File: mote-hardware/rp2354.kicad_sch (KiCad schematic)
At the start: 32 parts, among them J4 SM03B-SRSS-TB, J6 Conn_01x03_Pin, SW1 SW_Push, SW2 SW_Push, U1 RP2350_60QFN, U4 RP Radio Module 2, Y1 ABM8-272-T3

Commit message: Finish routing
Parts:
- J4: footprint Connector_JST:JST_SH_SM03B-SRSS-TB_1x03-1MP_P1.00mm_Horizontal -> Connector_JST:JST_SH_BM03B-SRSS-TB_1x03-1MP_P1.00mm_Vertical
- U1: value RP2350_60QFN -> RP2354_60QFN
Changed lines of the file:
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@@
 			)
 		)
-		(property "Value" "RP2350_60QFN"
+		(property "Value" "RP2354_60QFN"
 			(at 131.6833 172.72 0)
 			(effects
@@
 			)
 		)
-		(property "Footprint" "Connector_JST:JST_SH_SM03B-SRSS-TB_1x03-1MP_P1.00mm_Horizontal"
+		(property "Footprint" "Connector_JST:JST_SH_BM03B-SRSS-TB_1x03-1MP_P1.00mm_Vertical"
 			(at 294.64 213.36 0)
 			(effects

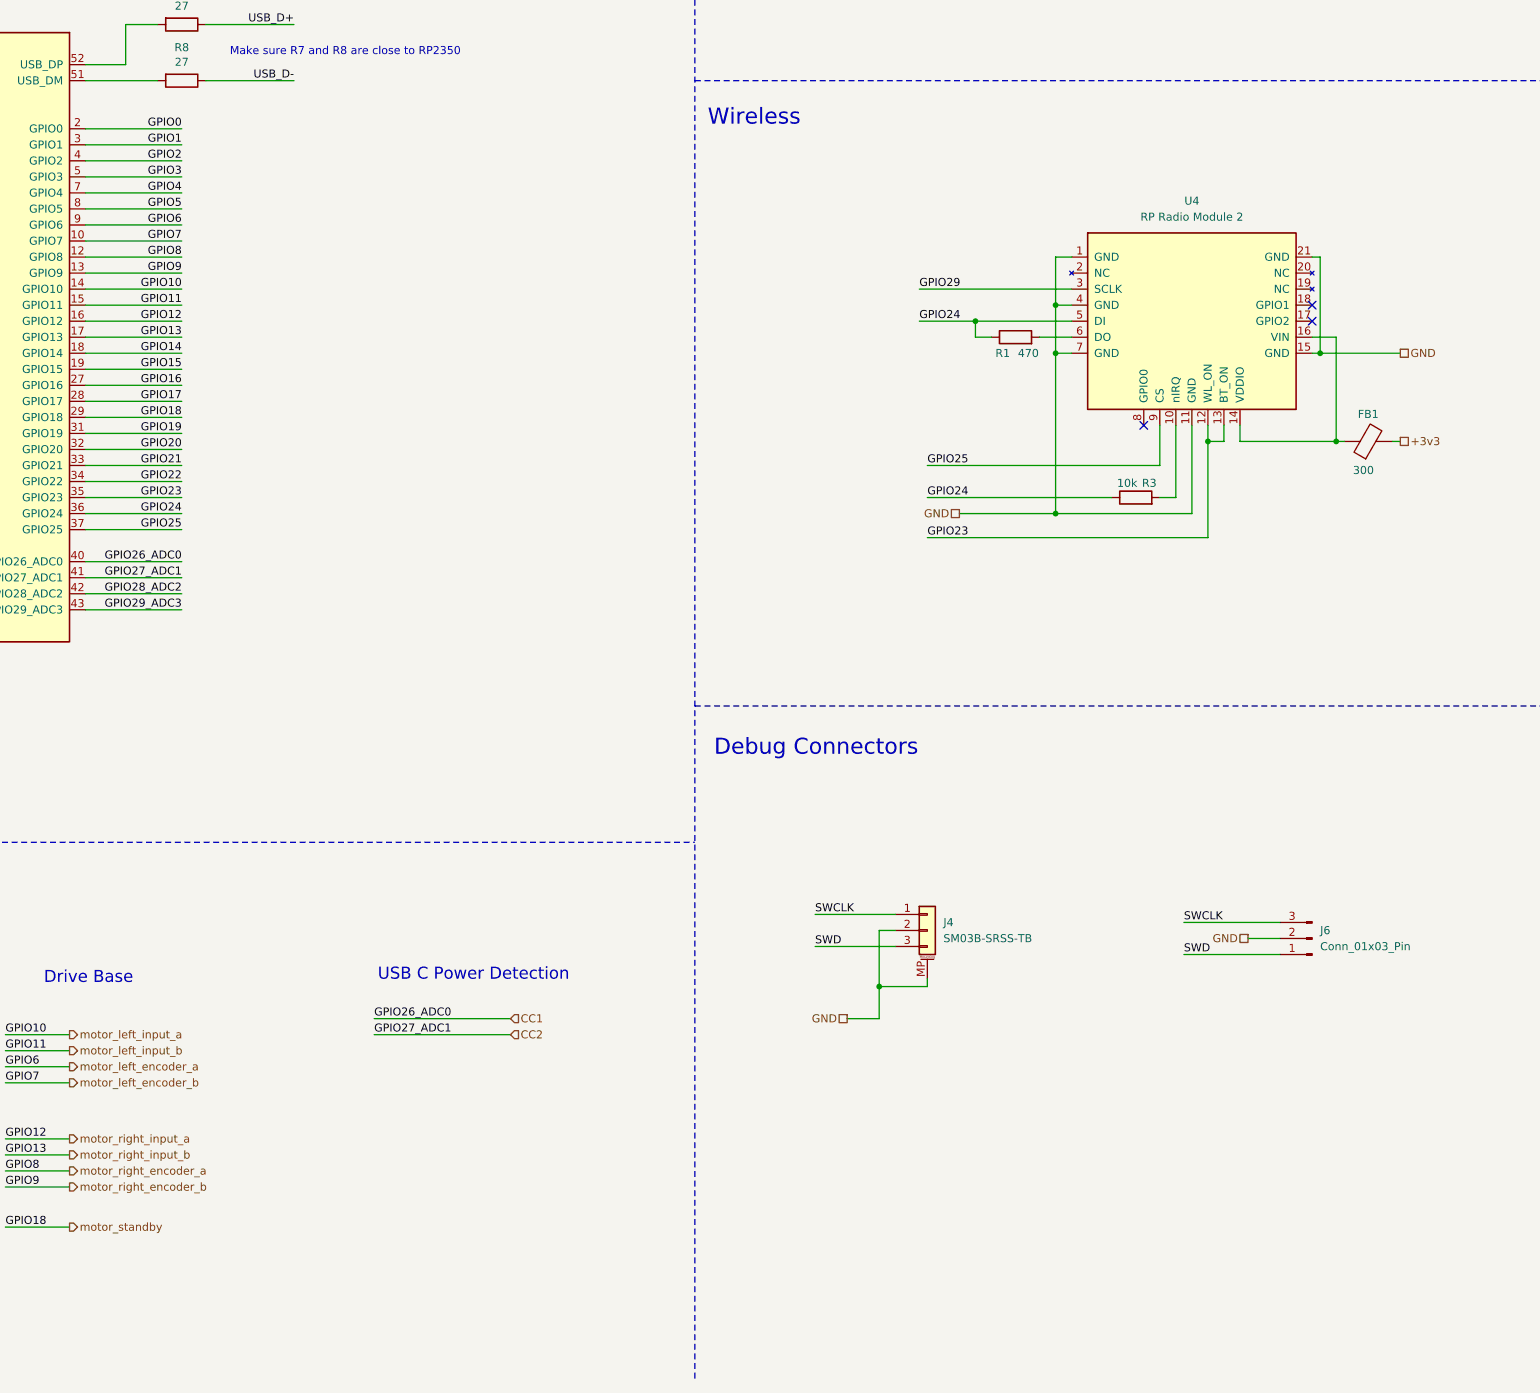
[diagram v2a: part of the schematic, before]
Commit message: Selecting LCSC components
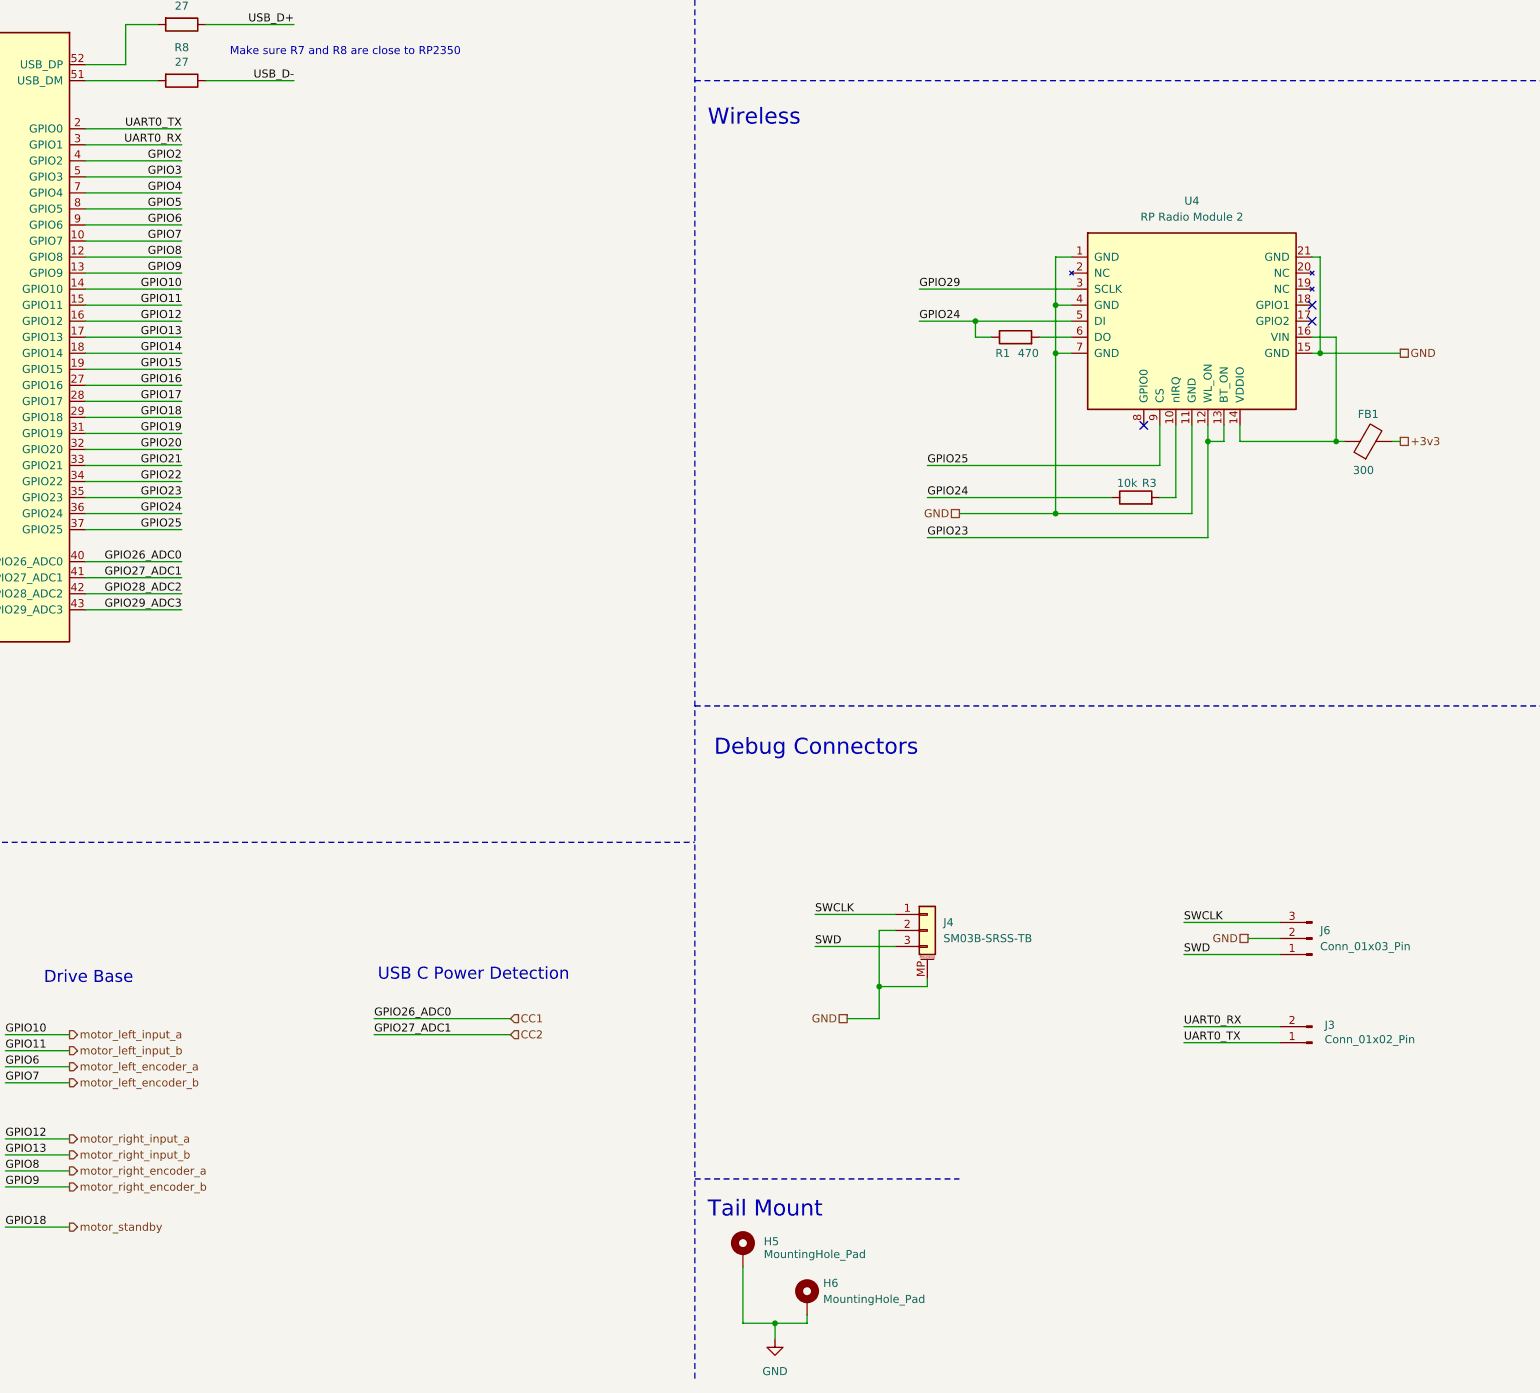
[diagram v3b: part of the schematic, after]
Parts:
- added H5, H6: MountingHole_Pad, MountingHole:MountingHole_4.3mm_M4_DIN965_Pad, symbol Mechanical:MountingHole_Pad
- added J3: Conn_01x02_Pin, Connector_PinHeader_2.54mm:PinHeader_1x02_P2.54mm_Vertical, symbol Connector:Conn_01x02_Pin
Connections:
- net GND: now also H5.1, H6.1
- net GPIO0 renamed UART0_TX
- net UART0_TX: now also J3.1 (Pin_1)
- net GPIO1 renamed UART0_RX
- net UART0_RX: now also J3.2 (Pin_2)
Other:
- note added: "Tail Mount"

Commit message: Finish selecting LCSC components
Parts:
- C10, C11, C12, C13, C14, C15, C16, C17, C18, C3, C4, C8, C9: footprint Capacitor_SMD:C_0402_1005Metric -> PCM_JLCPCB:C_0402
- R1, R2, R3, R4, R5, R6, R7, R8: footprint Resistor_SMD:R_0402_1005Metric -> PCM_JLCPCB:R_0402
- SW1, SW2: footprint Button_Switch_SMD:SW_Push_1P1T_NO_Vertical_Wuerth_434133025816 -> Button_Switch_SMD:SW_SPST_TS-1088-xR020
- Y1: footprint Crystal:Crystal_SMD_3225-4Pin_3.2x2.5mm -> PCM_JLCPCB:CRYSTAL-SMD_4P-L3.2-W2.5-BL
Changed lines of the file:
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@@
 			)
 		)
-		(property "Footprint" "Resistor_SMD:R_0402_1005Metric"
+		(property "Footprint" "PCM_JLCPCB:R_0402"
 			(at 176.53 68.072 90)
 			(effects
@@
 			)
 		)
-		(property "Footprint" "Resistor_SMD:R_0402_1005Metric"
+		(property "Footprint" "PCM_JLCPCB:R_0402"
 			(at 176.53 76.962 90)
 			(effects
@@
 			)
 		)
-		(property "Footprint" "Capacitor_SMD:C_0402_1005Metric"
+		(property "Footprint" "PCM_JLCPCB:C_0402"
 			(at 155.9052 44.45 0)
 			(effects
@@
 			)
 		)
-		(property "Footprint" "Capacitor_SMD:C_0402_1005Metric"
+		(property "Footprint" "PCM_JLCPCB:C_0402"
 			(at 167.3352 44.45 0)
 			(effects
@@
 			)
 		)
-		(property "Footprint" "Capacitor_SMD:C_0402_1005Metric"
+		(property "Footprint" "PCM_JLCPCB:C_0402"
 			(at 178.7652 44.45 0)
 			(effects
@@
 			)
 		)
-		(property "Footprint" "Capacitor_SMD:C_0402_1005Metric"
+		(property "Footprint" "PCM_JLCPCB:C_0402"
 			(at 190.1952 44.45 0)
 			(effects
@@
 			)
 		)
-		(property "Footprint" "Capacitor_SMD:C_0402_1005Metric"
+		(property "Footprint" "PCM_JLCPCB:C_0402"
 			(at 201.6252 44.45 0)
 			(effects
@@
 			)
 		)
-		(property "Footprint" "Capacitor_SMD:C_0402_1005Metric"
+		(property "Footprint" "PCM_JLCPCB:C_0402"
 			(at 213.0552 44.45 0)
 			(effects
@@
 			)
 		)
-		(property "Footprint" "Capacitor_SMD:C_0402_1005Metric"
+		(property "Footprint" "PCM_JLCPCB:C_0402"
 			(at 98.7552 44.45 0)
 			(effects
@@
 		)
 		(instances
-			(project ""
+			(project "mote-hardware"
 				(path "/94683f5c-9cd9-448e-be96-9792537b5cb8/8aa6d869-37ab-4fd7-8af1-9416ab877c54"
 					(reference "FB1")
@@
 			)
 		)
-		(property "Footprint" "Resistor_SMD:R_0402_1005Metric"
+		(property "Footprint" "PCM_JLCPCB:R_0402"
 			(at 52.07 137.922 90)
 			(effects
@@
 		)
 		(instances
-			(project ""
+			(project "mote-hardware"
 				(path "/94683f5c-9cd9-448e-be96-9792537b5cb8/8aa6d869-37ab-4fd7-8af1-9416ab877c54"
 					(reference "H5")
@@
 			)
 		)
-		(property "Footprint" "Capacitor_SMD:C_0402_1005Metric"
+		(property "Footprint" "PCM_JLCPCB:C_0402"
 			(at 224.4852 44.45 0)
 			(effects
@@
 			)
 		)
-		(property "Footprint" "Button_Switch_SMD:SW_Push_1P1T_NO_Vertical_Wuerth_434133025816"
+		(property "Footprint" "Button_Switch_SMD:SW_SPST_TS-1088-xR020"
 			(at 64.77 134.62 0)
 			(effects
@@
 			)
 		)
-		(property "Footprint" "Resistor_SMD:R_0402_1005Metric"
+		(property "Footprint" "PCM_JLCPCB:R_0402"
 			(at 75.565 96.012 90)
 			(effects
@@
 			)
 		)
-		(property "Footprint" "Resistor_SMD:R_0402_1005Metric"
+		(property "Footprint" "PCM_JLCPCB:R_0402"
 			(at 73.66 66.548 90)
 			(effects
@@
 			)
 		)
-		(property "Footprint" "Capacitor_SMD:C_0402_1005Metric"
+		(property "Footprint" "PCM_JLCPCB:C_0402"
 			(at 309.88 49.2252 0)
 			(effects
@@
 		)
 		(instances
-			(project ""
+			(project "mote-hardware"
 				(path "/94683f5c-9cd9-448e-be96-9792537b5cb8/8aa6d869-37ab-4fd7-8af1-9416ab877c54"
 					(reference "#PWR01")
@@
 			)
 		)
-		(property "Footprint" "Capacitor_SMD:C_0402_1005Metric"
+		(property "Footprint" "PCM_JLCPCB:C_0402"
 			(at 86.0552 73.66 0)
 			(effects
@@
 			)
 		)
-		(property "Footprint" "Resistor_SMD:R_0402_1005Metric"
+		(property "Footprint" "PCM_JLCPCB:R_0402"
 			(at 346.71 46.482 90)
 			(effects
@@
 			)
 		)
-		(property "Footprint" "Capacitor_SMD:C_0402_1005Metric"
+		(property "Footprint" "PCM_JLCPCB:C_0402"
 			(at 75.8952 44.45 0)
 			(effects
@@
 		)
 		(instances
-			(project ""
+			(project "mote-hardware"
 				(path "/94683f5c-9cd9-448e-be96-9792537b5cb8/8aa6d869-37ab-4fd7-8af1-9416ab877c54"
 					(reference "J3")
@@
 		)
 		(instances
-			(project ""
+			(project "mote-hardware"
 				(path "/94683f5c-9cd9-448e-be96-9792537b5cb8/8aa6d869-37ab-4fd7-8af1-9416ab877c54"
 					(reference "J6")
@@
 			)
 		)
-		(property "Footprint" "Button_Switch_SMD:SW_Push_1P1T_NO_Vertical_Wuerth_434133025816"
+		(property "Footprint" "Button_Switch_SMD:SW_SPST_TS-1088-xR020"
 			(at 53.34 105.41 0)
 			(effects
@@
 			)
 		)
-		(property "Footprint" "Capacitor_SMD:C_0402_1005Metric"
+		(property "Footprint" "PCM_JLCPCB:C_0402"
 			(at 87.3252 44.45 0)
 			(effects
@@
 			)
 		)
-		(property "Footprint" "Resistor_SMD:R_0402_1005Metric"
+		(property "Footprint" "PCM_JLCPCB:R_0402"
 			(at 327.66 146.558 90)
 			(effects
@@
 		)
 		(instances
-			(project ""
+			(project "mote-hardware"
 				(path "/94683f5c-9cd9-448e-be96-9792537b5cb8/8aa6d869-37ab-4fd7-8af1-9416ab877c54"
 					(reference "R3")
@@
 		)
 		(instances
-			(project ""
+			(project "mote-hardware"
 				(path "/94683f5c-9cd9-448e-be96-9792537b5cb8/8aa6d869-37ab-4fd7-8af1-9416ab877c54"
 					(reference "U4")
@@
 			)
 		)
-		(property "Footprint" "Crystal:Crystal_SMD_3225-4Pin_3.2x2.5mm"
+		(property "Footprint" "PCM_JLCPCB:CRYSTAL-SMD_4P-L3.2-W2.5-BL"
 			(at 328.93 43.18 0)
 			(effects
@@
 			)
 		)
-		(property "Footprint" "Resistor_SMD:R_0402_1005Metric"
+		(property "Footprint" "PCM_JLCPCB:R_0402"
 			(at 308.61 121.158 90)
 			(effects
@@
 		)
 		(instances
-			(project ""
+			(project "mote-hardware"
 				(path "/94683f5c-9cd9-448e-be96-9792537b5cb8/8aa6d869-37ab-4fd7-8af1-9416ab877c54"
 					(reference "R1")
@@
 			)
 		)
-		(property "Footprint" "Capacitor_SMD:C_0402_1005Metric"
+		(property "Footprint" "PCM_JLCPCB:C_0402"
 			(at 309.88 39.0652 0)
 			(effects

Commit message: Update date and github link
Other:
- company: github.com/usedhondacivic/mote -> github.com/empriselab/mote-core
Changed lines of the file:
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@@
 	(title_block
 		(title "Mote")
-		(date "2026-03-22")
+		(date "2026-03-31")
 		(rev "V0.0.0")
-		(company "github.com/usedhondacivic/mote")
+		(company "github.com/empriselab/mote-core")
 	)
 	(circle
